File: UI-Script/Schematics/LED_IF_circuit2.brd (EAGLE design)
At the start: 84 x 11.1 mm, 24 parts, among them Q1 MMBT5088, Q2 MMBT5088, Q3 MMBT5088, Q4 MMBT5088, Q5 MMBT5088

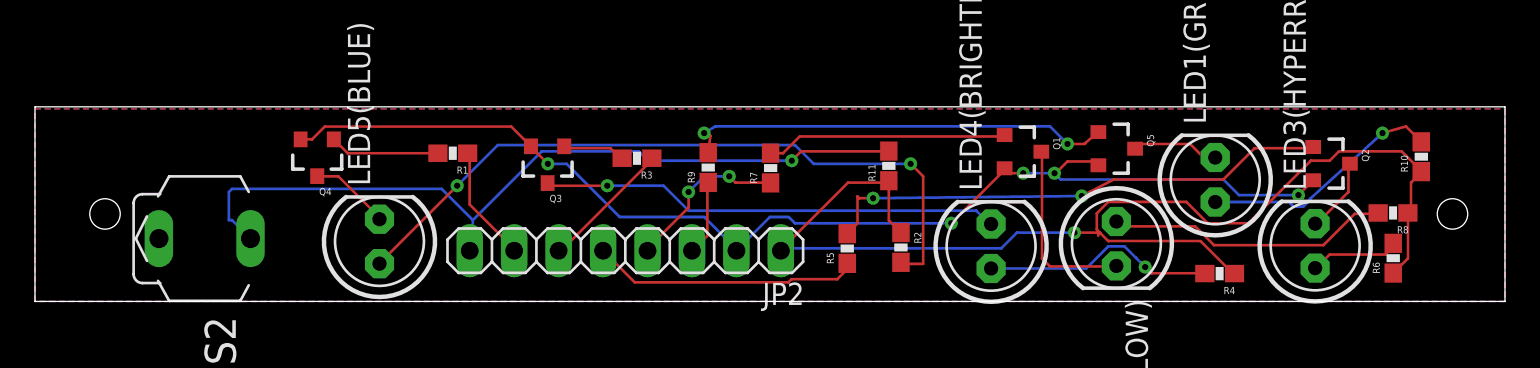
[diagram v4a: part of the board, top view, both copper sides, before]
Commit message: changed m2 hole a bit to be 4mm from top, since dimensions are 11x85mm. That way the switch is on the far end and more accessible under the slanted overhead from the 3DR
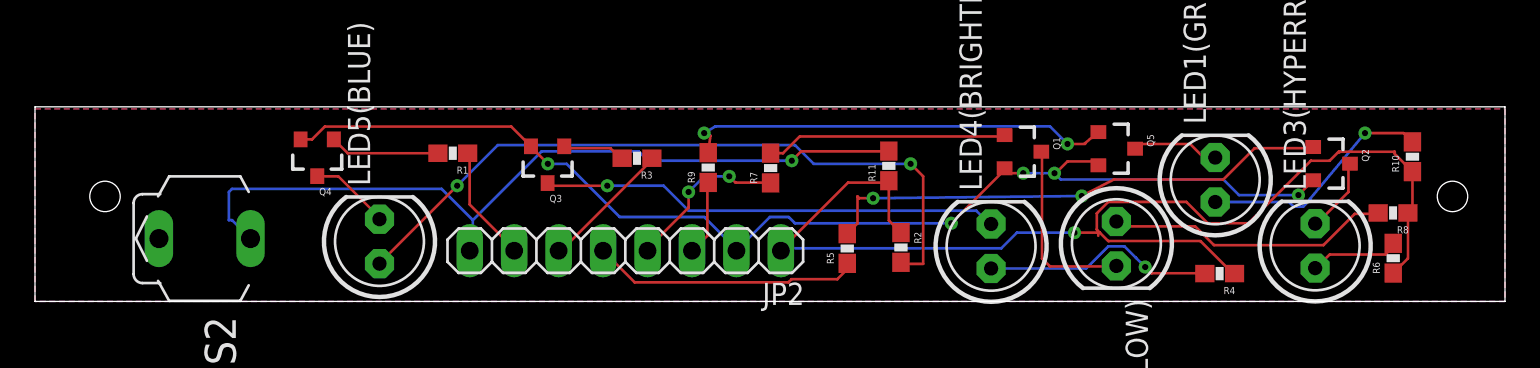
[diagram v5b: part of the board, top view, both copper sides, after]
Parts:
- moved R10 0.51 mm to (78.7, 8.27)
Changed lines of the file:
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@@
 <wire x1="84" y1="11.12" x2="0" y2="11.12" width="0" layer="20"/>
 <wire x1="0" y1="11.12" x2="0" y2="0" width="0" layer="20"/>
-<hole x="4" y="5" drill="1.74"/>
-<hole x="81" y="5" drill="1.74"/>
+<hole x="4" y="6" drill="1.74"/>
+<hole x="81" y="6" drill="1.74"/>
 </plain>
 <attributes>
@@
 </element>
 <element name="R1" library="SparkFun-Passives" package="0603-RES" value="1100" x="23.874" y="8.468" rot="R180"/>
-<element name="R10" library="SparkFun-Passives" package="0603-RES" value="55" x="79.219" y="8.269" rot="R90"/>
+<element name="R10" library="SparkFun-Passives" package="0603-RES" value="55" x="78.711" y="8.269" rot="R90"/>
 <element name="R11" library="SparkFun-Passives" package="0603-RES" value="1200" x="48.792" y="7.745" rot="R90"/>
 <element name="R2" library="SparkFun-Passives" package="0603-RES" value="55" x="49.482" y="3.085" rot="R270"/>
@@
 <wire x1="42.7093" y1="3.0379" x2="42.622" y2="2.898" width="0.1524" layer="1"/>
 <wire x1="77.613" y1="1.621" x2="77.3771" y2="1.2509" width="0.1524" layer="1"/>
-<wire x1="78.4493" y1="5.0036" x2="78.455" y2="5.057" width="0.1524" layer="1"/>
+<wire x1="78.455" y1="5.057" x2="78.4493" y2="5.0036" width="0.1524" layer="1"/>
 <wire x1="60.758" y1="3.7527" x2="60.758" y2="3.9314" width="0.1524" layer="1"/>
 <wire x1="67.0125" y1="4.4675" x2="69.3356" y2="4.4675" width="0.1524" layer="1"/>
 <wire x1="72.9096" y1="8.0415" x2="69.3356" y2="4.4675" width="0.1524" layer="1"/>
 <wire x1="73.9818" y1="8.0415" x2="72.9096" y2="8.0415" width="0.1524" layer="1"/>
-<wire x1="74.5179" y1="8.5776" x2="73.9818" y2="8.0415" width="0.1524" layer="1"/>
-<wire x1="78.0919" y1="8.5776" x2="74.5179" y2="8.5776" width="0.1524" layer="1"/>
-<wire x1="79.1641" y1="7.5054" x2="78.0919" y2="8.5776" width="0.1524" layer="1"/>
+<wire x1="74.5179" y1="8.5776" x2="74.47015" y2="8.52985" width="0.1524" layer="1"/>
+<wire x1="74.47015" y1="8.52985" x2="73.9818" y2="8.0415" width="0.1524" layer="1"/>
 <wire x1="68.545" y1="1.589" x2="68.4421" y2="1.6083" width="0.1524" layer="1"/>
-<wire x1="79.1641" y1="7.5054" x2="79.219" y2="7.419" width="0.1524" layer="1"/>
-<wire x1="79.1641" y1="7.3267" x2="78.628" y2="6.7906" width="0.1524" layer="1"/>
 <wire x1="78.628" y1="5.1823" x2="78.455" y2="5.057" width="0.1524" layer="1"/>
-<wire x1="79.1641" y1="7.3267" x2="79.219" y2="7.419" width="0.1524" layer="1"/>
 <wire x1="55.2183" y1="3.0379" x2="42.7093" y2="3.0379" width="0.1524" layer="16"/>
 <wire x1="56.1118" y1="3.9314" x2="55.2183" y2="3.0379" width="0.1524" layer="16"/>
@@
 <wire x1="42.7093" y1="3.0379" x2="42.622" y2="2.898" width="0.1524" layer="16"/>
 <via x="59.4006" y="3.9314" extent="1-16" drill="0.35"/>
-<wire x1="78.628" y1="6.7906" x2="78.628" y2="5.23" width="0.1524" layer="1"/>
-<wire x1="78.628" y1="5.23" x2="78.455" y2="5.057" width="0.1524" layer="1"/>
 <wire x1="78.455" y1="5.057" x2="78.455" y2="2.463" width="0.1524" layer="1"/>
 <wire x1="78.455" y1="2.463" x2="77.613" y2="1.621" width="0.1524" layer="1"/>
 <wire x1="48.792" y1="6.895" x2="48.792" y2="4.625" width="0.1524" layer="1"/>
 <wire x1="48.792" y1="4.625" x2="49.482" y2="3.935" width="0.1524" layer="1"/>
-<wire x1="60.8894625" y1="3.8894625" x2="61.329325" y2="3.4496" width="0.1524" layer="1"/>
-<wire x1="60.8894625" y1="3.8894625" x2="60.6736" y2="4.105325" width="0.1524" layer="1"/>
+<wire x1="60.847525" y1="3.9314" x2="61.329325" y2="3.4496" width="0.1524" layer="1"/>
+<wire x1="60.847525" y1="3.9314" x2="60.6736" y2="4.105325" width="0.1524" layer="1"/>
 <wire x1="60.6736" y1="4.105325" x2="60.6736" y2="5.032675" width="0.1524" layer="1"/>
 <wire x1="60.6736" y1="5.032675" x2="61.329325" y2="5.6884" width="0.1524" layer="1"/>
@@
 <wire x1="65.7916" y1="5.6884" x2="67.0125" y2="4.4675" width="0.1524" layer="1"/>
 <wire x1="60.758" y1="3.9314" x2="60.847525" y2="3.9314" width="0.1524" layer="1"/>
-<wire x1="60.847525" y1="3.9314" x2="60.8894625" y2="3.8894625" width="0.1524" layer="1"/>
+<wire x1="74.47015" y1="8.52985" x2="74.549175" y2="8.52985" width="0.1524" layer="1"/>
+<wire x1="74.549175" y1="8.52985" x2="74.574525" y2="8.5552" width="0.1524" layer="1"/>
+<wire x1="74.574525" y1="8.5552" x2="77.7018" y2="8.5552" width="0.1524" layer="1"/>
+<wire x1="78.838" y1="5.3923" x2="78.4493" y2="5.0036" width="0.1524" layer="1"/>
+<wire x1="77.7018" y1="8.5552" x2="77.7018" y2="8.4282" width="0.1524" layer="1"/>
+<wire x1="77.7018" y1="8.4282" x2="78.711" y2="7.419" width="0.1524" layer="1"/>
+<wire x1="78.711" y1="7.419" x2="78.711" y2="5.313" width="0.1524" layer="1"/>
+<wire x1="78.711" y1="5.313" x2="78.455" y2="5.057" width="0.1524" layer="1"/>
 </signal>
 <signal name="N$6">
 <contactref element="LED1(GREEN)" pad="A"/>
 <contactref element="R10" pad="2"/>
-<wire x1="79.219" y1="9.119" x2="78.338" y2="10" width="0.1524" layer="1"/>
-<wire x1="78.338" y1="10" x2="77" y2="9.619" width="0.1524" layer="1"/>
-<via x="77" y="9.619" extent="1-16" drill="0.35"/>
-<wire x1="77" y1="9.619" x2="72.8542" y2="5.8542" width="0.1524" layer="16"/>
+<via x="76" y="9.619" extent="1-16" drill="0.35"/>
+<wire x1="76" y1="9.619" x2="72.8542" y2="5.8542" width="0.1524" layer="16"/>
 <wire x1="72.8542" y1="5.8542" x2="72.8542" y2="5.8026625" width="0.1524" layer="16"/>
 <wire x1="72.8542" y1="5.8026625" x2="72.4679375" y2="5.4164" width="0.1524" layer="16"/>
@@
 <wire x1="71.9216625" y1="5.4164" x2="71.6560625" y2="5.682" width="0.1524" layer="16"/>
 <wire x1="71.6560625" y1="5.682" x2="67.442" y2="5.682" width="0.1524" layer="16"/>
+<wire x1="78.711" y1="9.119" x2="79" y2="9.281" width="0.1524" layer="1"/>
+<wire x1="76" y1="9.619" x2="78.211" y2="9.619" width="0.1524" layer="1"/>
+<wire x1="78.211" y1="9.619" x2="78.711" y2="9.119" width="0.1524" layer="1"/>
 </signal>
 <signal name="N$8">
